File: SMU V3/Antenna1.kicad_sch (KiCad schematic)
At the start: 9 parts, among them J3 SMA

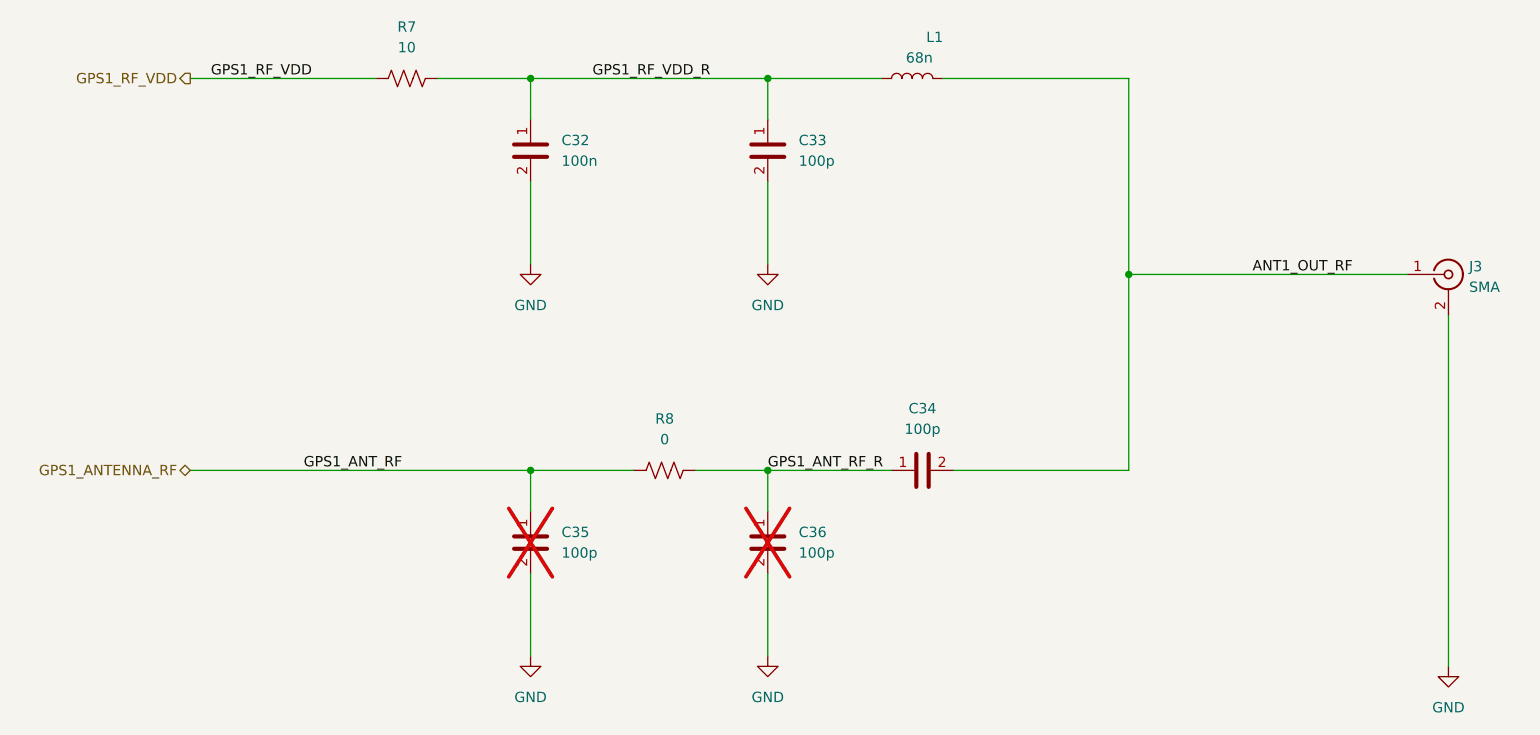
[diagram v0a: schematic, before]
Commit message: improved V3
added uart/spi test points and status leds
removed main 3v3 ldo
added silkscreen
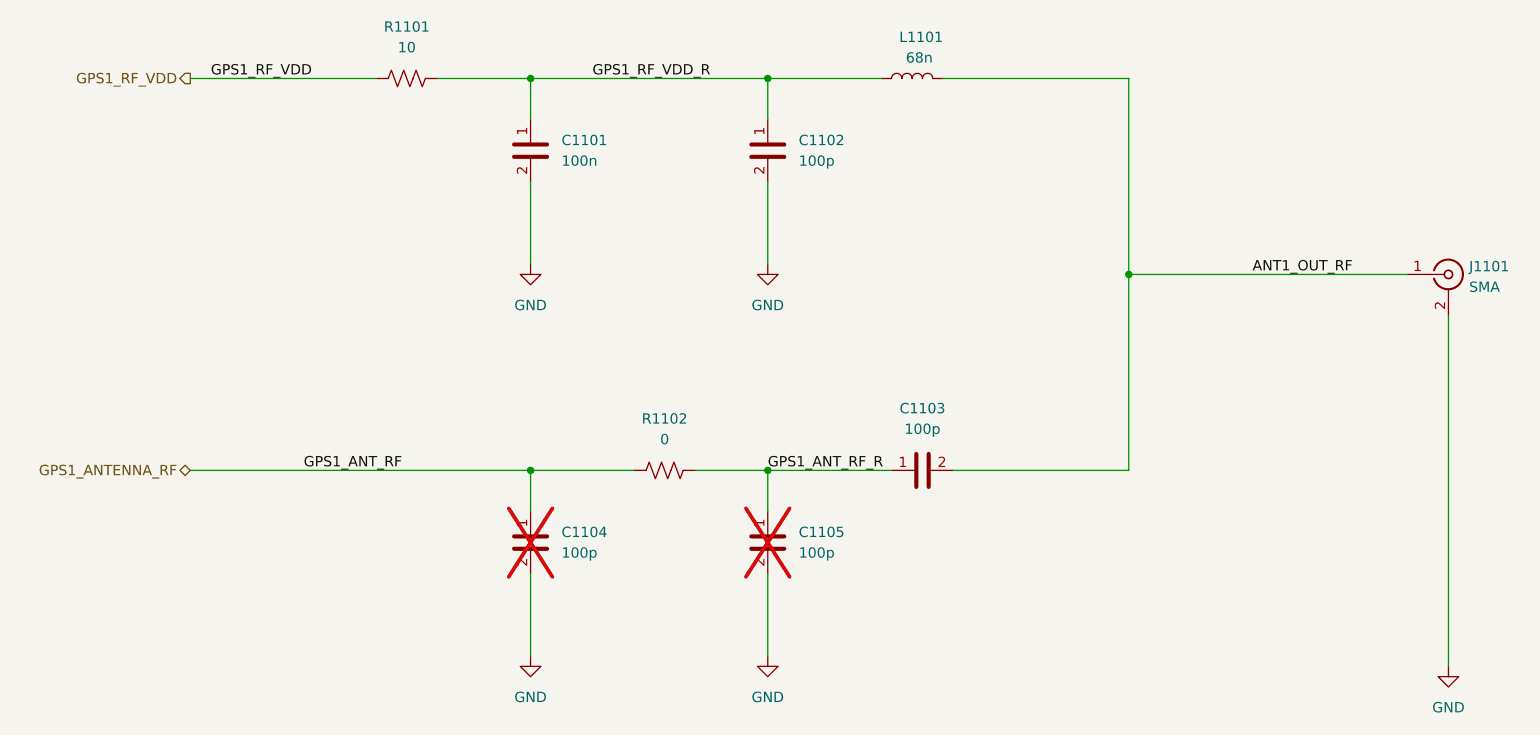
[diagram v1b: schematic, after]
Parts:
- renumbered C32 to C1101, C33 to C1102, C34 to C1103, C35 to C1104, C36 to C1105, J3 to J1101, L1 to L1101, R7 to R1101, R8 to R1102
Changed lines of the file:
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@@
 		(in_pos_files yes)
 		(dnp no)
-		(property "Reference" "L1"
+		(property "Reference" "L1101"
 			(at 203.2 31.75 0)
 			(show_name no)
@@
 			(project "SMU V3"
 				(path "/1f58b889-96e6-4877-90a3-5a655db5910b/9f4b7fd8-1b41-49c1-882f-9b0abe430a88"
-					(reference "L1")
+					(reference "L1101")
 					(unit 1)
 				)
@@
 		(dnp no)
 		(fields_autoplaced yes)
-		(property "Reference" "#PWR030"
+		(property "Reference" "#PWR01104"
 			(at 181.61 114.3 0)
 			(hide yes)
@@
 			(project "SMU V3"
 				(path "/1f58b889-96e6-4877-90a3-5a655db5910b/9f4b7fd8-1b41-49c1-882f-9b0abe430a88"
-					(reference "#PWR030")
+					(reference "#PWR01104")
 					(unit 1)
 				)
@@
 		(dnp yes)
 		(fields_autoplaced yes)
-		(property "Reference" "C36"
+		(property "Reference" "C1105"
 			(at 185.42 92.7099 0)
 			(show_name no)
@@
 			(project "SMU V3"
 				(path "/1f58b889-96e6-4877-90a3-5a655db5910b/9f4b7fd8-1b41-49c1-882f-9b0abe430a88"
-					(reference "C36")
+					(reference "C1105")
 					(unit 1)
 				)
@@
 		(dnp no)
 		(fields_autoplaced yes)
-		(property "Reference" "R7"
+		(property "Reference" "R1101"
 			(at 137.16 30.48 0)
 			(show_name no)
@@
 			(project "SMU V3"
 				(path "/1f58b889-96e6-4877-90a3-5a655db5910b/9f4b7fd8-1b41-49c1-882f-9b0abe430a88"
-					(reference "R7")
+					(reference "R1101")
 					(unit 1)
 				)
@@
 		(dnp no)
 		(fields_autoplaced yes)
-		(property "Reference" "#PWR029"
+		(property "Reference" "#PWR01102"
 			(at 181.61 66.04 0)
 			(hide yes)
@@
 			(project "SMU V3"
 				(path "/1f58b889-96e6-4877-90a3-5a655db5910b/9f4b7fd8-1b41-49c1-882f-9b0abe430a88"
-					(reference "#PWR029")
+					(reference "#PWR01102")
 					(unit 1)
 				)
@@
 		(dnp no)
 		(fields_autoplaced yes)
-		(property "Reference" "#PWR027"
+		(property "Reference" "#PWR01101"
 			(at 152.4 66.04 0)
 			(hide yes)
@@
 			(project "SMU V3"
 				(path "/1f58b889-96e6-4877-90a3-5a655db5910b/9f4b7fd8-1b41-49c1-882f-9b0abe430a88"
-					(reference "#PWR027")
+					(reference "#PWR01101")
 					(unit 1)
 				)
@@
 		(dnp yes)
 		(fields_autoplaced yes)
-		(property "Reference" "C35"
+		(property "Reference" "C1104"
 			(at 156.21 92.7099 0)
 			(show_name no)
@@
 			(project "SMU V3"
 				(path "/1f58b889-96e6-4877-90a3-5a655db5910b/9f4b7fd8-1b41-49c1-882f-9b0abe430a88"
-					(reference "C35")
+					(reference "C1104")
 					(unit 1)
 				)
@@
 		(dnp no)
 		(fields_autoplaced yes)
-		(property "Reference" "C32"
+		(property "Reference" "C1101"
 			(at 156.21 44.4499 0)
 			(show_name no)
@@
 			(project "SMU V3"
 				(path "/1f58b889-96e6-4877-90a3-5a655db5910b/9f4b7fd8-1b41-49c1-882f-9b0abe430a88"
-					(reference "C32")
+					(reference "C1101")
 					(unit 1)
 				)
@@
 		(dnp no)
 		(fields_autoplaced yes)
-		(property "Reference" "#PWR028"
+		(property "Reference" "#PWR01103"
 			(at 152.4 114.3 0)
 			(hide yes)
@@
 			(project "SMU V3"
 				(path "/1f58b889-96e6-4877-90a3-5a655db5910b/9f4b7fd8-1b41-49c1-882f-9b0abe430a88"
-					(reference "#PWR028")
+					(reference "#PWR01103")
 					(unit 1)
 				)
@@
 		(dnp no)
 		(fields_autoplaced yes)
-		(property "Reference" "#PWR031"
+		(property "Reference" "#PWR01105"
 			(at 265.43 115.57 0)
 			(hide yes)
@@
 			(project "SMU V3"
 				(path "/1f58b889-96e6-4877-90a3-5a655db5910b/9f4b7fd8-1b41-49c1-882f-9b0abe430a88"
-					(reference "#PWR031")
+					(reference "#PWR01105")
 					(unit 1)
 				)
@@
 		(dnp no)
 		(fields_autoplaced yes)
-		(property "Reference" "J3"
+		(property "Reference" "J1101"
 			(at 267.97 59.9831 0)
 			(show_name no)
@@
 			(project "SMU V3"
 				(path "/1f58b889-96e6-4877-90a3-5a655db5910b/9f4b7fd8-1b41-49c1-882f-9b0abe430a88"
-					(reference "J3")
+					(reference "J1101")
 					(unit 1)
 				)
@@
 		(dnp no)
 		(fields_autoplaced yes)
-		(property "Reference" "C34"
+		(property "Reference" "C1103"
 			(at 200.66 77.47 90)
 			(show_name no)
@@
 			(project "SMU V3"
 				(path "/1f58b889-96e6-4877-90a3-5a655db5910b/9f4b7fd8-1b41-49c1-882f-9b0abe430a88"
-					(reference "C34")
+					(reference "C1103")
 					(unit 1)
 				)
@@
 		(dnp no)
 		(fields_autoplaced yes)
-		(property "Reference" "C33"
+		(property "Reference" "C1102"
 			(at 185.42 44.4499 0)
 			(show_name no)
@@
 			(project "SMU V3"
 				(path "/1f58b889-96e6-4877-90a3-5a655db5910b/9f4b7fd8-1b41-49c1-882f-9b0abe430a88"
-					(reference "C33")
+					(reference "C1102")
 					(unit 1)
 				)
@@
 		(dnp no)
 		(fields_autoplaced yes)
-		(property "Reference" "R8"
+		(property "Reference" "R1102"
 			(at 168.91 78.74 0)
 			(show_name no)
@@
 			(project "SMU V3"
 				(path "/1f58b889-96e6-4877-90a3-5a655db5910b/9f4b7fd8-1b41-49c1-882f-9b0abe430a88"
-					(reference "R8")
+					(reference "R1102")
 					(unit 1)
 				)
